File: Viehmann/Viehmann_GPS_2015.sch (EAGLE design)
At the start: 16 parts, among them J1 U.FL

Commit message: Added 3-Pin Connector
Give this a look Judah and let me know if you need more stuffs
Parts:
- removed C4: 1uF, SparkFun-Capacitors:CAP1206
- removed U$1: V_REG_LD1117#50, SparkFun-PowerIC:V_REG_MIC2920
- removed VIN: M02PTH, SparkFun-Connectors:M02PTH
- added U$2: MLX-3-PIN, MRDT-2015-General:MLX-3-PIN
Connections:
- removed net VIN: C4.1, U$1.IN, VIN.1
- net 5V: now also U$2.5V; no longer U$1.OUT
- net GND: now also U$2.GND; no longer C4.2, U$1.GND, VIN.2
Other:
- moved on the sheet: C5

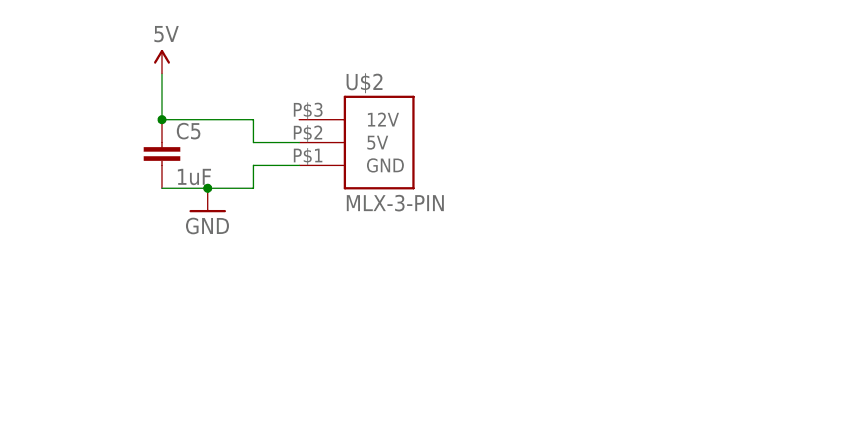
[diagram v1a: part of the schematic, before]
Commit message: swapped power conn to app45 and put backup battery on top, gen'ed gerbers
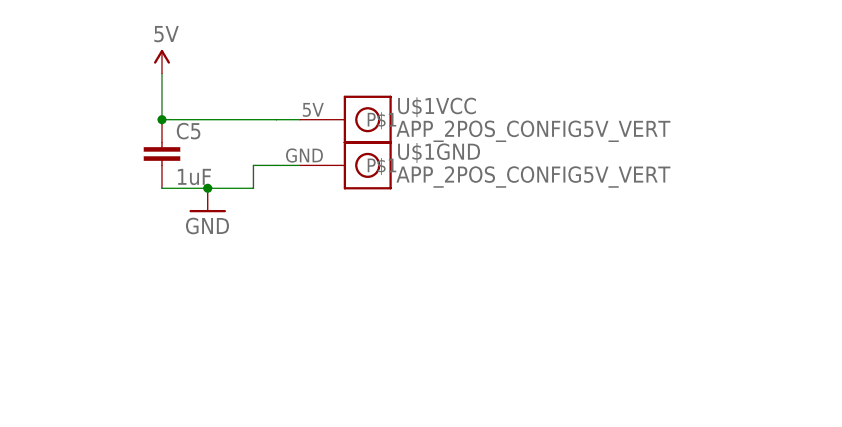
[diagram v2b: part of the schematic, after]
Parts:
- removed U$2: MLX-3-PIN, MRDT-2015-General:MLX-3-PIN
- added U$1: APP_2POS_CONFIG5V_VERT, MRDT-Connectors:APP_2POS_CONFIG5V_VERT
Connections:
- net 5V: now also U$1VCC.P$1; no longer U$2.5V
- net GND: now also U$1GND.P$1; no longer U$2.GND
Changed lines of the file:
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@@
 <?xml version="1.0" encoding="utf-8"?>
 <!DOCTYPE eagle SYSTEM "eagle.dtd">
-<eagle version="6.6.0">
+<eagle version="6.5.0">
 <drawing>
 <settings>
@@
 <layers>
 <layer number="1" name="Top" color="4" fill="1" visible="no" active="no"/>
+<layer number="2" name="Route2" color="1" fill="3" visible="no" active="no"/>
+<layer number="3" name="Route3" color="4" fill="3" visible="no" active="no"/>
+<layer number="4" name="Route4" color="1" fill="4" visible="no" active="no"/>
+<layer number="5" name="Route5" color="4" fill="4" visible="no" active="no"/>
+<layer number="6" name="Route6" color="1" fill="8" visible="no" active="no"/>
+<layer number="7" name="Route7" color="4" fill="8" visible="no" active="no"/>
+<layer number="8" name="Route8" color="1" fill="2" visible="no" active="no"/>
+<layer number="9" name="Route9" color="4" fill="2" visible="no" active="no"/>
+<layer number="10" name="Route10" color="1" fill="7" visible="no" active="no"/>
+<layer number="11" name="Route11" color="4" fill="7" visible="no" active="no"/>
+<layer number="12" name="Route12" color="1" fill="5" visible="no" active="no"/>
+<layer number="13" name="Route13" color="4" fill="5" visible="no" active="no"/>
+<layer number="14" name="Route14" color="1" fill="6" visible="no" active="no"/>
+<layer number="15" name="Route15" color="4" fill="6" visible="no" active="no"/>
 <layer number="16" name="Bottom" color="1" fill="1" visible="no" active="no"/>
 <layer number="17" name="Pads" color="2" fill="1" visible="no" active="no"/>
@@
 <part name="SUPPLY4" library="SparkFun-Aesthetics" deviceset="5V" device=""/>
 <part name="C5" library="SparkFun-Capacitors" deviceset="CAP" device="1206" value="1uF"/>
-<part name="U$2" library="MRDT-2015-General" deviceset="MLX-3-PIN" device=""/>
 <part name="SUPPLY3" library="SparkFun-Aesthetics" deviceset="5V" device=""/>
 <part name="GND8" library="SparkFun-Aesthetics" deviceset="GND" device=""/>
 <part name="SUPPLY1" library="SparkFun-Aesthetics" deviceset="3.3V" device=""/>
 <part name="SUPPLY2" library="SparkFun-Aesthetics" deviceset="3.3V" device=""/>
+<part name="U$1" library="MRDT-Connectors" deviceset="APP_2POS_CONFIG" device="5V_VERT"/>
 </parts>
 <sheets>
@@
 <instance part="SUPPLY4" gate="G$1" x="7.62" y="114.3"/>
 <instance part="C5" gate="G$1" x="73.66" y="132.08"/>
-<instance part="U$2" gate="G$1" x="96.52" y="134.62"/>
 <instance part="SUPPLY3" gate="G$1" x="73.66" y="142.24"/>
 <instance part="GND8" gate="1" x="78.74" y="127"/>
 <instance part="SUPPLY1" gate="G$1" x="30.48" y="91.44"/>
 <instance part="SUPPLY2" gate="G$1" x="-22.86" y="114.3"/>
+<instance part="U$1" gate="GND" x="96.52" y="132.08"/>
+<instance part="U$1" gate="VCC" x="96.52" y="137.16"/>
 </instances>
 <busses>
@@
 </segment>
 <segment>
-<pinref part="U$2" gate="G$1" pin="GND"/>
-<wire x1="88.9" y1="132.08" x2="83.82" y2="132.08" width="0.1524" layer="91"/>
+<wire x1="86.36" y1="132.08" x2="83.82" y2="132.08" width="0.1524" layer="91"/>
 <wire x1="83.82" y1="132.08" x2="83.82" y2="129.54" width="0.1524" layer="91"/>
 <pinref part="C5" gate="G$1" pin="2"/>
@@
 <wire x1="78.74" y1="129.54" x2="73.66" y2="129.54" width="0.1524" layer="91"/>
 <junction x="78.74" y="129.54"/>
+<pinref part="U$1" gate="GND" pin="P$1"/>
+<wire x1="86.36" y1="132.08" x2="88.9" y2="132.08" width="0.1524" layer="91"/>
 </segment>
 </net>
@@
 </segment>
 <segment>
-<pinref part="U$2" gate="G$1" pin="5V"/>
-<wire x1="88.9" y1="134.62" x2="83.82" y2="134.62" width="0.1524" layer="91"/>
-<wire x1="83.82" y1="134.62" x2="83.82" y2="137.16" width="0.1524" layer="91"/>
 <pinref part="C5" gate="G$1" pin="1"/>
-<wire x1="83.82" y1="137.16" x2="73.66" y2="137.16" width="0.1524" layer="91"/>
 <pinref part="SUPPLY3" gate="G$1" pin="5V"/>
+<wire x1="86.36" y1="137.16" x2="73.66" y2="137.16" width="0.1524" layer="91"/>
 <wire x1="73.66" y1="142.24" x2="73.66" y2="137.16" width="0.1524" layer="91"/>
 <junction x="73.66" y="137.16"/>
-</segment>
-</net>
+<pinref part="U$1" gate="VCC" pin="P$1"/>
+<wire x1="86.36" y1="137.16" x2="88.9" y2="137.16" width="0.1524" layer="91"/>
+</segment>
+</net>
